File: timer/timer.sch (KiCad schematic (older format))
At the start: 21 parts

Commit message: More changes
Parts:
- added P4: PWR, symbol CONN_01X02
- added P6: Encoder, symbol CONN_01X04
- added U1: 74HC595, symbol 74HC595
- gave numbers to parts that had none: 21
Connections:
- net +5V: now also C5.2, U2.15 (VIN), P4.2 (P2), P6.1 (P1), U1.16 (VCC)
- net GND: now also U2.14 (GND), P4.1 (P1), P6.4 (P4), U1.13 (G), U1.8 (GND)
- net R1: now also U2.6 (D16); no longer U2.4 (D14)
- net R2: now also U2.7 (D17); no longer U2.5 (D15)
- net R3: now also U2.10 (D20); no longer U2.7 (D17)
- net R4: now also U2.11 (D21); no longer U2.22 (D4)
- net SRCLR: now reaches U2.24 (aD6)
- net SRCLR: now also U1.10 (SRCLR)
- net at U2.25 (D7): now also P6.3 (P3)
- net at U2.26 (D8): now also P6.2 (P2); no longer P5.2 (P2)
- net at U2.27 (aD9): now also P5.2 (P2)
- removed net C1: P1.1 (P1), P1.10 (P10), U2.11 (D21), U2.6 (D16)
- removed net C2: P1.13 (P13), P1.4 (P4), U2.23 (aD5), U2.3 (AREF)
- removed net C3: P1.14 (P14), P1.2 (P2), U2.10 (D20), U2.21 (aD3)
- net C4: no longer names the net of U2.20 (aD2)
- net C4: no longer P1.7 (P7)
- new net 1C1: P1.1 (P1), U1.15 (QA)
- new net 1C2: P1.4 (P4), U1.1 (QB)
- new net 1C3: P1.2 (P2), U1.2 (QC)
- new net 1C4: P1.7 (P7), U1.3 (QD)
- new net 2C1: P1.10 (P10), U1.4 (QE)
- new net 2C2: P1.13 (P13), U1.5 (QF)
- new net 2C3: P1.14 (P14), U1.6 (QG)
- new net RCLK: U1.12 (RCLK), U2.23 (aD5)
- new net SER: U1.14 (SER), U2.5 (D15)
- new net SRCLK: U1.11 (SRCLK), U2.4 (D14)
- no-connect marks 0 -> 27
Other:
- moved on the sheet: C1, C2, C3, C4, C5, C6, C7, C8, P1, P2, P3, P5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

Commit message: More changes
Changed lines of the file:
@@
 L +5V #PWR019
 U 1 1 5E25E2E7
-P 5000 2150
-F 0 "#PWR019" H 5000 2000 50  0001 C CNN
-F 1 "+5V" H 5000 2290 50  0000 C CNN
-F 2 "" H 5000 2150 50  0000 C CNN
-F 3 "" H 5000 2150 50  0000 C CNN
-	1    5000 2150
+P 5150 2150
+F 0 "#PWR019" H 5150 2000 50  0001 C CNN
+F 1 "+5V" H 5150 2290 50  0000 C CNN
+F 2 "" H 5150 2150 50  0000 C CNN
+F 3 "" H 5150 2150 50  0000 C CNN
+	1    5150 2150
 	1    0    0    -1
 $EndComp
@@
 L GND #PWR021
 U 1 1 5E25EC43
-P 6700 2150
-F 0 "#PWR021" H 6700 1900 50  0001 C CNN
-F 1 "GND" H 6700 2000 50  0000 C CNN
-F 2 "" H 6700 2150 50  0000 C CNN
-F 3 "" H 6700 2150 50  0000 C CNN
-	1    6700 2150
+P 6600 2150
+F 0 "#PWR021" H 6600 1900 50  0001 C CNN
+F 1 "GND" H 6600 2000 50  0000 C CNN
+F 2 "" H 6600 2150 50  0000 C CNN
+F 3 "" H 6600 2150 50  0000 C CNN
+	1    6600 2150
 	1    0    0    -1
 $EndComp
@@
 	3050 2400 3050 2050
 Wire Wire Line
-	4250 3600 4750 3600
+	4250 3600 4550 3600
+Wire Wire Line
+	4550 3600 4750 3600
 Wire Wire Line
 	4250 3600 4250 2300
@@
 	7500 2800 7500 2900
 Wire Wire Line
-	8950 3500 9200 3500
+	8950 3500 9150 3500
+Wire Wire Line
+	9150 3500 9200 3500
 Wire Wire Line
 	8950 3800 9100 3800
@@
 	7150 3700 7900 3700
 Wire Wire Line
-	6700 4000 6700 4100
+	6700 4000 6700 4050
+Wire Wire Line
+	6700 4050 6700 4100
 Wire Wire Line
 	6700 4950 6700 5150
@@
 	6400 4800 6400 4400
 Wire Wire Line
-	6400 4400 6850 4400
+	6400 4400 6700 4400
+Wire Wire Line
+	6700 4400 6850 4400
 Wire Wire Line
 	3500 4900 6500 4900
@@
 	6500 4900 6500 4650
 Wire Wire Line
-	6500 4650 6850 4650
+	6500 4650 6700 4650
+Wire Wire Line
+	6700 4650 6850 4650
 Connection ~ 6700 4650
 Connection ~ 6700 4050
@@
 	9050 3900 9050 4450
 Wire Wire Line
-	9050 4450 9650 4450
+	9050 4450 9400 4450
+Wire Wire Line
+	9400 4450 9650 4450
 Connection ~ 9400 4450
 Connection ~ 9650 4450
@@
 	9650 4450 9650 4550
 Wire Wire Line
-	9400 4850 9950 4850
-Wire Wire Line
-	9950 4650 9950 4900
+	9400 4850 9650 4850
+Wire Wire Line
+	9650 4850 9950 4850
+Wire Wire Line
+	9950 4650 9950 4850
+Wire Wire Line
+	9950 4850 9950 4900
 Connection ~ 9950 4850
 Connection ~ 9650 4850
@@
 	6450 4050 6700 4050
 Wire Wire Line
-	5000 2150 5400 2150
+	5150 2150 5400 2150
 Wire Wire Line
 	5750 3200 6200 3200
@@
 	3850 3400 4150 3400
 Wire Bus Line
-	1850 2800 1850 4500
-Wire Bus Line
-	4550 4500 4550 3200
+	1850 2800 1850 3000
+Wire Bus Line
+	1850 3000 1850 3100
+Wire Bus Line
+	1850 3100 1850 3200
+Wire Bus Line
+	1850 3200 1850 3300
+Wire Bus Line
+	1850 3300 1850 3400
+Wire Bus Line
+	1850 3400 1850 3500
+Wire Bus Line
+	1850 3500 1850 3700
+Wire Bus Line
+	1850 3700 1850 4000
+Wire Bus Line
+	1850 4000 1850 4100
+Wire Bus Line
+	1850 4100 1850 4200
+Wire Bus Line
+	1850 4200 1850 4300
+Wire Bus Line
+	1850 4300 1850 4500
+Wire Bus Line
+	4550 4500 4550 3700
+Wire Bus Line
+	4550 3700 4550 3600
+Wire Bus Line
+	4550 3600 4550 3300
+Wire Bus Line
+	4550 3300 4550 3200
 Entry Wire Line
 	1750 2900 1850 3000
@@
 Connection ~ 2250 4500
 Wire Bus Line
-	2250 3300 2250 4500
+	2250 3300 2250 3400
+Wire Bus Line
+	2250 3400 2250 3500
+Wire Bus Line
+	2250 3500 2250 3600
+Wire Bus Line
+	2250 3600 2250 3700
+Wire Bus Line
+	2250 3700 2250 3800
+Wire Bus Line
+	2250 3800 2250 3900
+Wire Bus Line
+	2250 3900 2250 4500
 Entry Wire Line
 	2250 3900 2350 4000
@@
 RCLK
 Wire Bus Line
-	1850 4500 4550 4500
+	1850 4500 2250 4500
+Wire Bus Line
+	2250 4500 4550 4500
 Entry Wire Line
 	4550 3200 4650 3300
@@
 	7900 2800 7900 2600
 Wire Wire Line
-	6700 2150 6400 2150
+	6600 2150 6400 2150
 Wire Wire Line
 	7900 4100 7500 4100

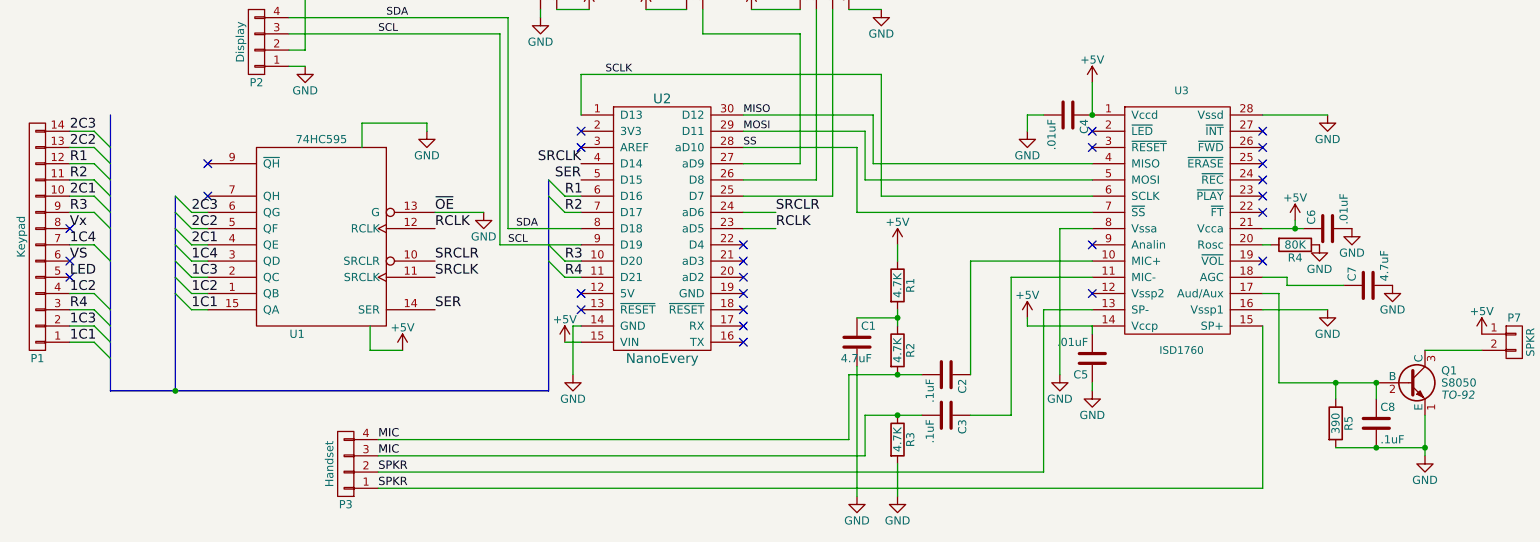
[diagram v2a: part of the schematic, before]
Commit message: Refactor code, added namespaces
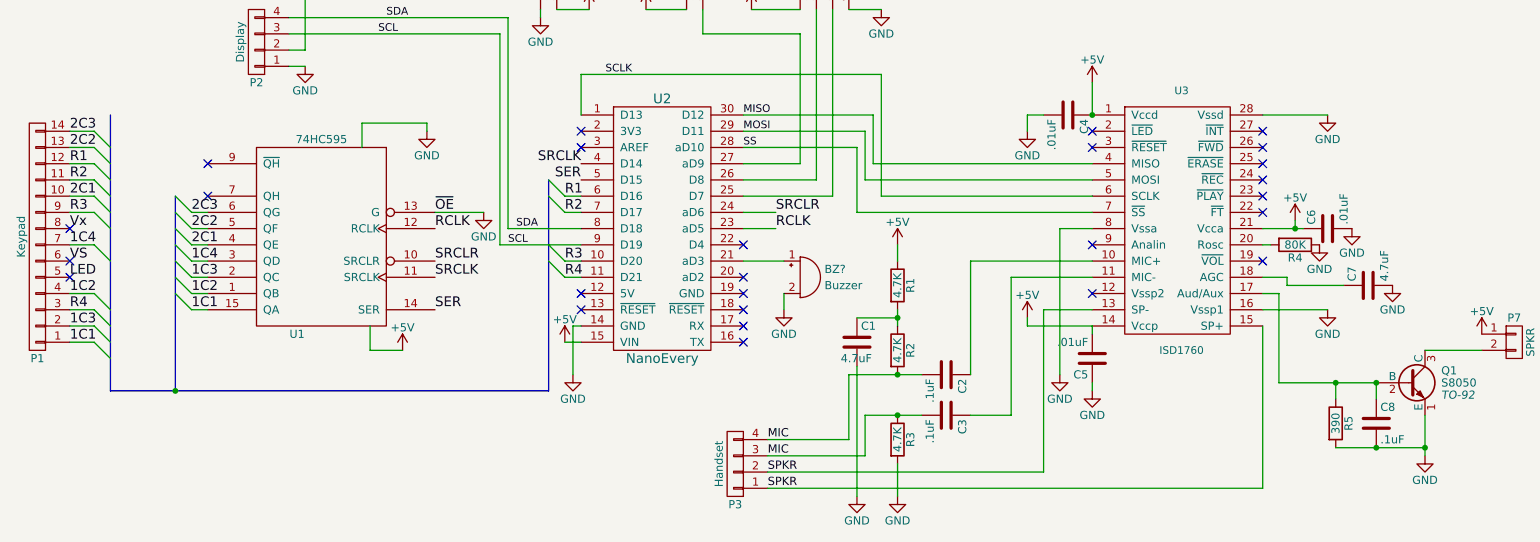
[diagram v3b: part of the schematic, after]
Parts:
- added BZ?: Buzzer, symbol Buzzer
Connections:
- net GND: now also BZ?.2 (+)
- net at U2.21 (aD3): now also BZ?.1 (-)
- no-connect marks 27 -> 26
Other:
- moved on the sheet: P3
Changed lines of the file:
@@
 L CONN_01X04 P3
 U 1 1 5E255360
-P 3300 4950
-F 0 "P3" H 3300 5200 50  0000 C CNN
-F 1 "Handset" V 3400 4950 50  0000 C CNN
-F 2 "" H 3300 4950 50  0000 C CNN
-F 3 "" H 3300 4950 50  0000 C CNN
-	1    3300 4950
+P 5700 4950
+F 0 "P3" H 5700 5200 50  0000 C CNN
+F 1 "Handset" V 5800 4950 50  0000 C CNN
+F 2 "" H 5700 4950 50  0000 C CNN
+F 3 "" H 5700 4950 50  0000 C CNN
+	1    5700 4950
 	-1   0    0    1
 $EndComp
@@
 	1    0    0    -1
 $EndComp
-Text Label 3500 5100 0    51   ~ 0
+Text Label 5900 5100 0    51   ~ 0
 SPKR
-Text Label 3500 5000 0    51   ~ 0
+Text Label 5900 5000 0    51   ~ 0
 SPKR
-Text Label 3500 4900 0    51   ~ 0
+Text Label 5900 4900 0    51   ~ 0
 MIC
-Text Label 3500 4800 0    51   ~ 0
+Text Label 5900 4800 0    51   ~ 0
 MIC
 $Comp
@@
 	3050 2400 3050 2050
 Wire Wire Line
-	4250 3600 4550 3600
-Wire Wire Line
-	4550 3600 4750 3600
+	4250 3600 4750 3600
 Wire Wire Line
 	4250 3600 4250 2300
@@
 	7500 2800 7500 2900
 Wire Wire Line
-	8950 3500 9150 3500
-Wire Wire Line
-	9150 3500 9200 3500
+	8950 3500 9200 3500
 Wire Wire Line
 	8950 3800 9100 3800
@@
 	7600 4000 7600 5000
 Wire Wire Line
-	7600 5000 3500 5000
+	7600 5000 5900 5000
 Wire Wire Line
 	8950 4100 8950 5100
 Wire Wire Line
-	8950 5100 3500 5100
+	8950 5100 5900 5100
 Wire Wire Line
 	7150 3700 7150 4400
@@
 	7150 3700 7900 3700
 Wire Wire Line
-	6700 4000 6700 4050
-Wire Wire Line
-	6700 4050 6700 4100
+	6700 4000 6700 4100
 Wire Wire Line
 	6700 4950 6700 5150
 Wire Wire Line
-	3500 4800 6400 4800
+	5900 4800 6400 4800
 Wire Wire Line
 	6400 4800 6400 4400
 Wire Wire Line
-	6400 4400 6700 4400
-Wire Wire Line
-	6700 4400 6850 4400
-Wire Wire Line
-	3500 4900 6500 4900
+	6400 4400 6850 4400
+Wire Wire Line
+	5900 4900 6500 4900
 Wire Wire Line
 	6500 4900 6500 4650
 Wire Wire Line
-	6500 4650 6700 4650
-Wire Wire Line
-	6700 4650 6850 4650
+	6500 4650 6850 4650
 Connection ~ 6700 4650
 Connection ~ 6700 4050
@@
 	9050 3900 9050 4450
 Wire Wire Line
-	9050 4450 9400 4450
-Wire Wire Line
-	9400 4450 9650 4450
+	9050 4450 9650 4450
 Connection ~ 9400 4450
 Connection ~ 9650 4450
@@
 	9650 4450 9650 4550
 Wire Wire Line
-	9400 4850 9650 4850
-Wire Wire Line
-	9650 4850 9950 4850
-Wire Wire Line
-	9950 4650 9950 4850
-Wire Wire Line
-	9950 4850 9950 4900
+	9400 4850 9950 4850
+Wire Wire Line
+	9950 4650 9950 4900
 Connection ~ 9950 4850
 Connection ~ 9650 4850
@@
 	3850 3400 4150 3400
 Wire Bus Line
-	1850 2800 1850 3000
+	1850 2800 1850 4500
 Wire Bus Line
-	1850 3000 1850 3100
-Wire Bus Line
-	1850 3100 1850 3200
-Wire Bus Line
-	1850 3200 1850 3300
-Wire Bus Line
-	1850 3300 1850 3400
-Wire Bus Line
-	1850 3400 1850 3500
-Wire Bus Line
-	1850 3500 1850 3700
-Wire Bus Line
-	1850 3700 1850 4000
-Wire Bus Line
-	1850 4000 1850 4100
-Wire Bus Line
-	1850 4100 1850 4200
-Wire Bus Line
-	1850 4200 1850 4300
-Wire Bus Line
-	1850 4300 1850 4500
-Wire Bus Line
-	4550 4500 4550 3700
-Wire Bus Line
-	4550 3700 4550 3600
-Wire Bus Line
-	4550 3600 4550 3300
-Wire Bus Line
-	4550 3300 4550 3200
+	4550 4500 4550 3200
 Entry Wire Line
 	1750 2900 1850 3000
@@
 Connection ~ 2250 4500
 Wire Bus Line
-	2250 3300 2250 3400
-Wire Bus Line
-	2250 3400 2250 3500
-Wire Bus Line
-	2250 3500 2250 3600
-Wire Bus Line
-	2250 3600 2250 3700
-Wire Bus Line
-	2250 3700 2250 3800
-Wire Bus Line
-	2250 3800 2250 3900
-Wire Bus Line
-	2250 3900 2250 4500
+	2250 3300 2250 4500
 Entry Wire Line
 	2250 3900 2350 4000
@@
 RCLK
 Wire Bus Line
-	1850 4500 2250 4500
-Wire Bus Line
-	2250 4500 4550 4500
+	1850 4500 4550 4500
 Entry Wire Line
 	4550 3200 4650 3300
@@
 NoConn ~ 5750 3900
 NoConn ~ 5750 3800
-NoConn ~ 5750 3700
 NoConn ~ 5750 3600
 NoConn ~ 4750 3000
@@
 Wire Wire Line
 	7900 4150 7900 4100
+$Comp
+L Buzzer BZ?
+U 1 1 5E27DCA2
+P 6100 3800
+F 0 "BZ?" H 6250 3850 50  0000 L CNN
+F 1 "Buzzer" H 6250 3750 50  0000 L CNN
+F 2 "" V 6075 3900 50  0000 C CNN
+F 3 "" V 6075 3900 50  0000 C CNN
+	1    6100 3800
+	1    0    0    -1
+$EndComp
+Wire Wire Line
+	5750 3700 6000 3700
+$Comp
+L GND #PWR?
+U 1 1 5E27DE4E
+P 6000 4000
+F 0 "#PWR?" H 6000 3750 50  0001 C CNN
+F 1 "GND" H 6000 3850 50  0000 C CNN
+F 2 "" H 6000 4000 50  0000 C CNN
+F 3 "" H 6000 4000 50  0000 C CNN
+	1    6000 4000
+	1    0    0    -1
+$EndComp
+Wire Wire Line
+	6000 3900 6000 4000
 $EndSCHEMATC

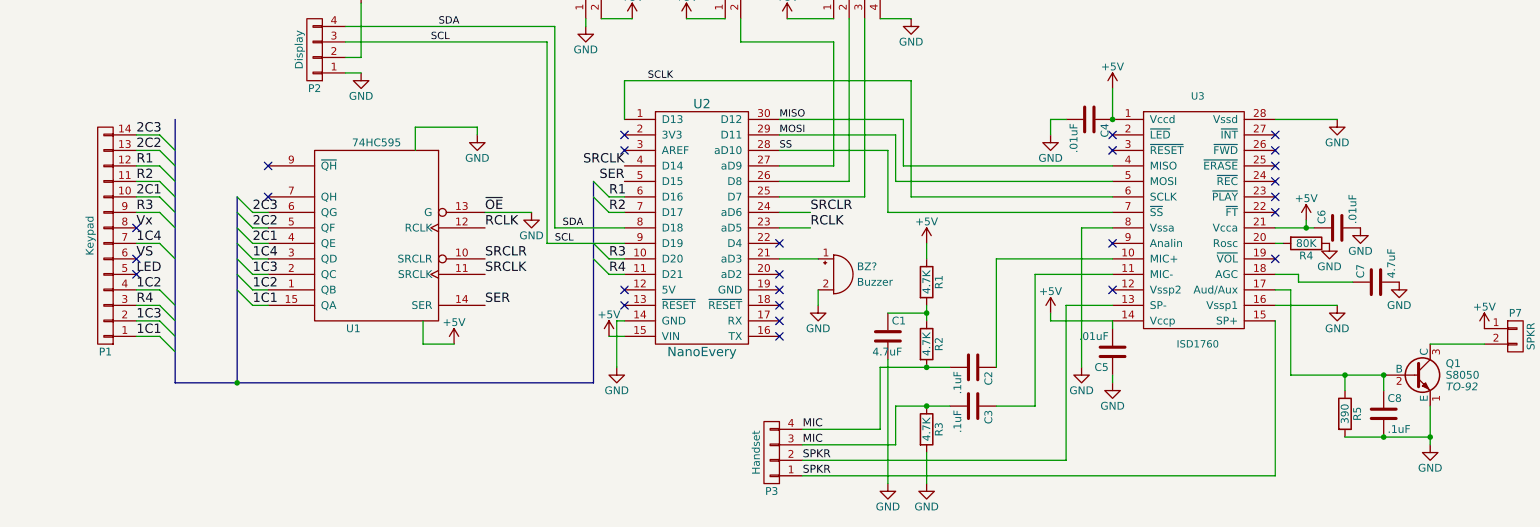
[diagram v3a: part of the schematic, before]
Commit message: Added pull down resistors
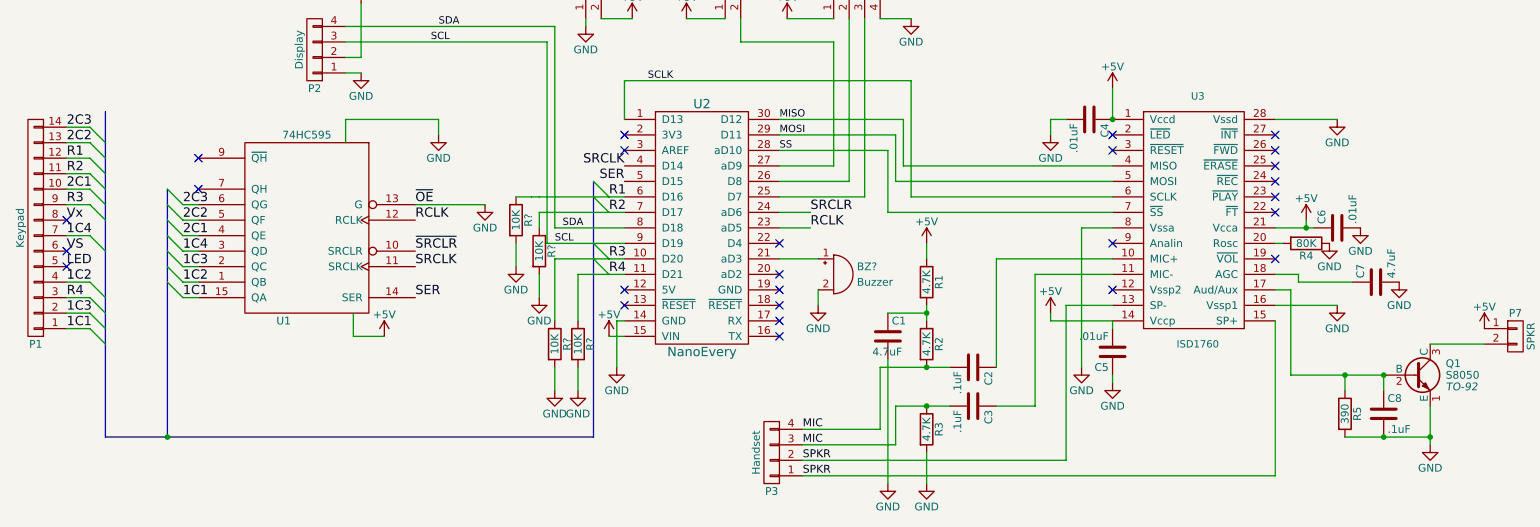
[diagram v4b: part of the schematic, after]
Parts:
- added R? (x4): 10K, symbol R
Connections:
- net GND: now also R?.2, R?.2, R?.2, R?.2
- net R1: now also R?.1
- net R2: now also R?.1
- net R3: now also R?.1
- net R4: now also R?.1
- net SRCLR: no longer U1.10 (SRCLR)
- new net ~SRCLR: U1.10 (SRCLR)
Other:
- moved on the sheet: P1, U1
